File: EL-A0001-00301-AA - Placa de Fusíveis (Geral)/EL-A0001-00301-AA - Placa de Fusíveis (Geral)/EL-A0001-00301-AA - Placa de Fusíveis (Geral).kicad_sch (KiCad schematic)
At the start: 30 parts, among them J1 1-776087-1, J10 AUX_POWER, J2 AUX_1, J3 AUX_2, J4 DC_CONVERTER, J5 VBAT, J6 UNFUSED, J7 CS_POWER, J8 ECU_POWER, J9 ISOL_POWER, U1 TJA1050-Module

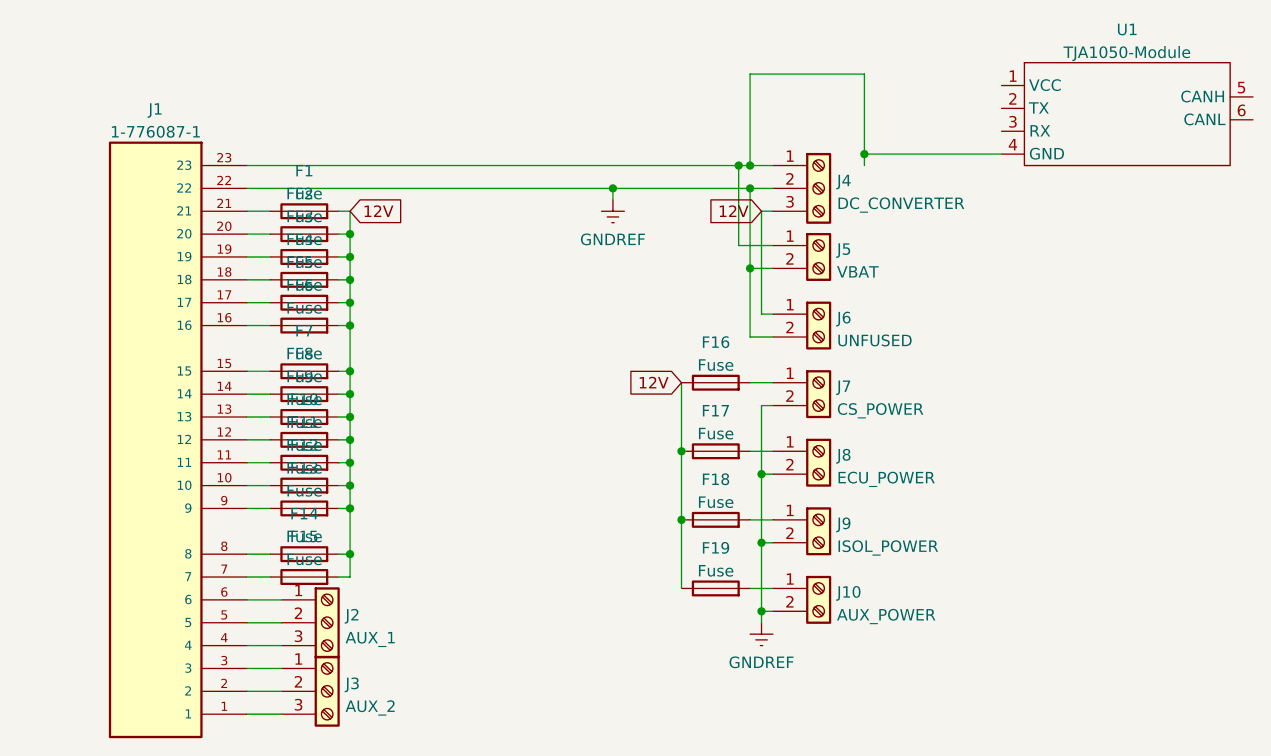
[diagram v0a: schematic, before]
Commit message: MOD: placa de fusiveis
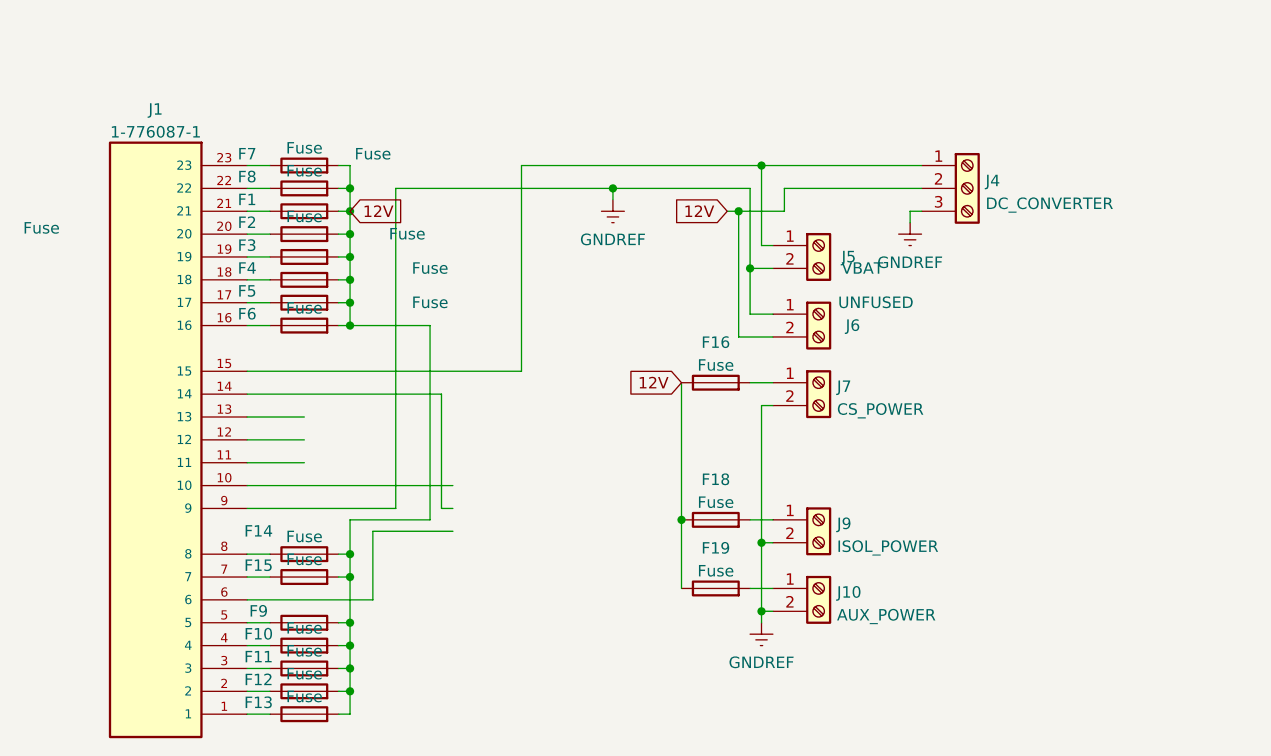
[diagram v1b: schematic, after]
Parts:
- removed F17: Fuse, Fuse:Fuseholder_Cylinder-5x20mm_Schurter_0031_8201_Horizontal_Open, symbol Device:Fuse
- removed J2: AUX_1, TerminalBlock:TerminalBlock_bornier-3_P5.08mm, symbol Connector:Screw_Terminal_01x03
- removed J3: AUX_2, TerminalBlock:TerminalBlock_bornier-3_P5.08mm, symbol Connector:Screw_Terminal_01x03
- removed J8: ECU_POWER, TerminalBlock:TerminalBlock_bornier-2_P5.08mm, symbol Connector:Screw_Terminal_01x02
- removed U1: TJA1050-Module, Cheetah:TJA1050-Module, symbol Cheetah:TJA1050-Module
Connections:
- net 12V: now also J4.2 (Pin_2), J6.2 (Pin_2); no longer J4.3 (Pin_3), J6.1 (Pin_1)
- net GNDREF: now also J1.9, J4.3 (Pin_3), J6.1 (Pin_1); no longer J1.22, J4.2 (Pin_2), J6.2 (Pin_2)
- net at F9.1: now also J1.5; no longer J1.13
- net at J4.1 (Pin_1), J5.1 (Pin_1): now also J1.15; no longer J1.23
- net at F12.1: now also J1.2; no longer J1.10
- net at F8.1: now also J1.22; no longer J1.14
- net at J1.4: now also F10.1
- net at J1.3: now also F11.1
- net at J1.1: now also F13.1
- net at J1.12: no longer F10.1
- net at F7.1: now also J1.23; no longer J1.15
- net at J1.11: no longer F11.1
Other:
- moved on the sheet: F10, F11, F12, F13, F7, F8, F9

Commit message: ADD: fusiveis
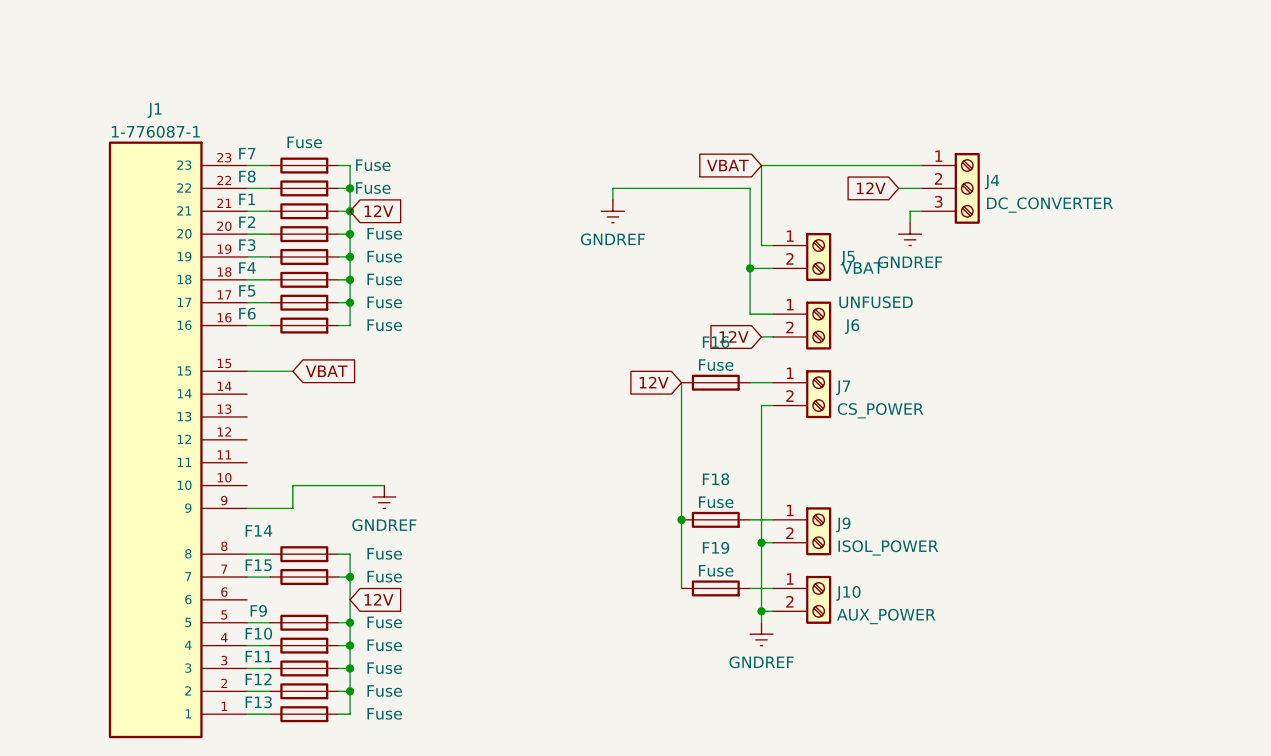
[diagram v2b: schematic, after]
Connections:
- net VBAT: now reaches J1.15, J4.1 (Pin_1), J5.1 (Pin_1)
